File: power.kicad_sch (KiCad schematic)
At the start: 13 parts

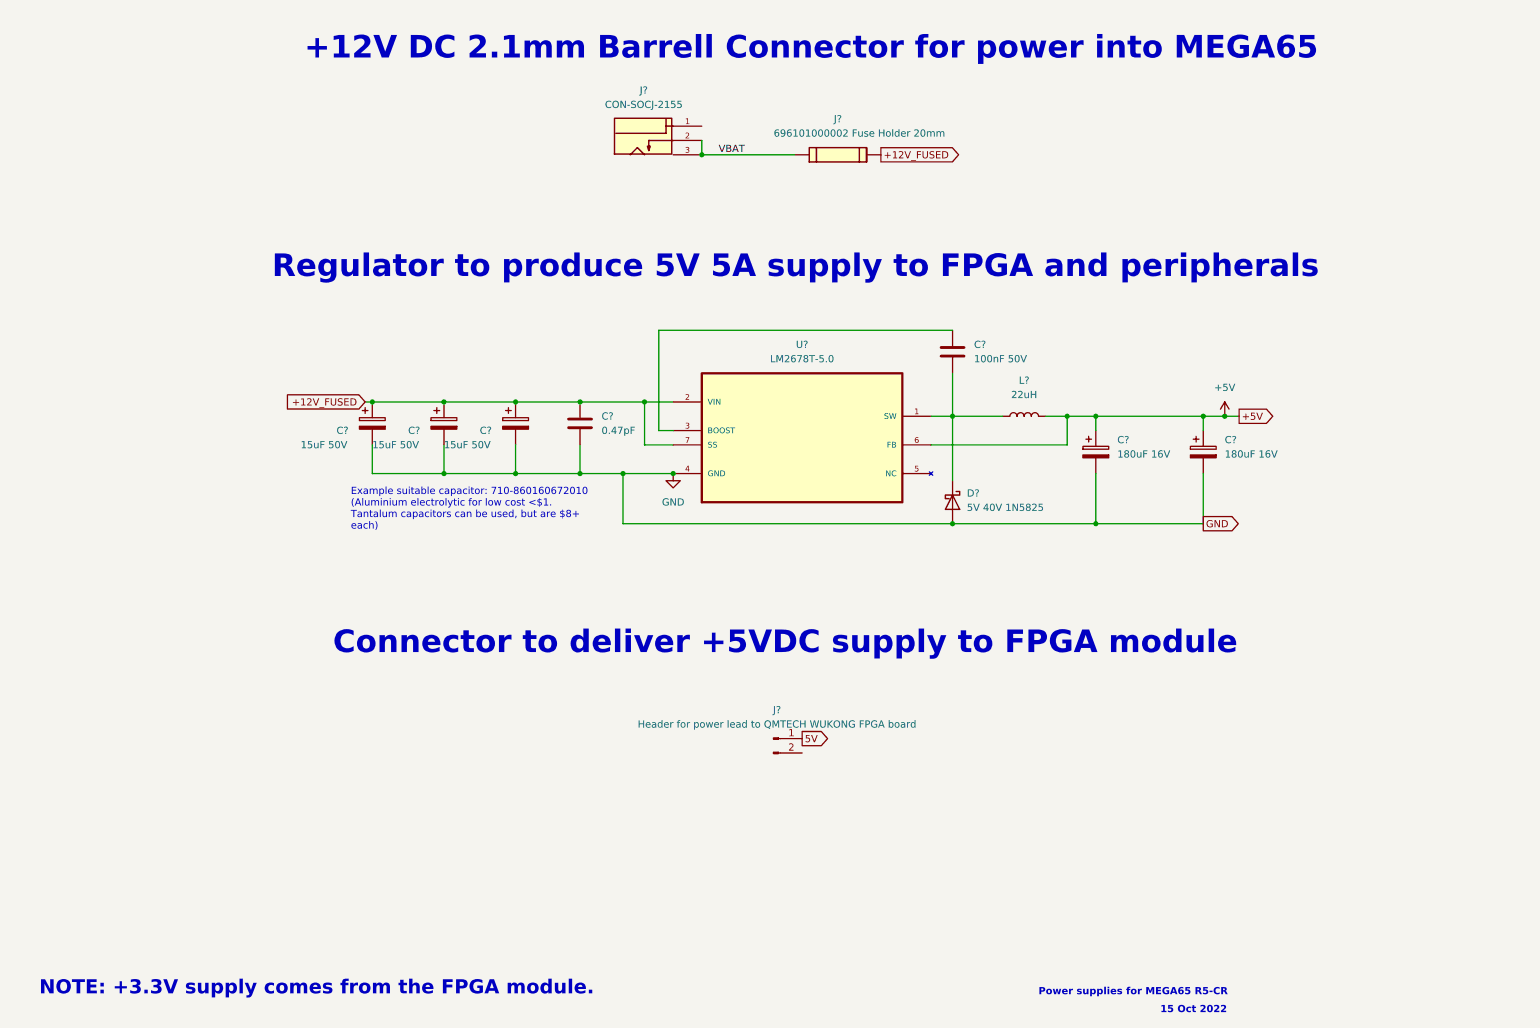
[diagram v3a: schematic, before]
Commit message: add all missing footprints
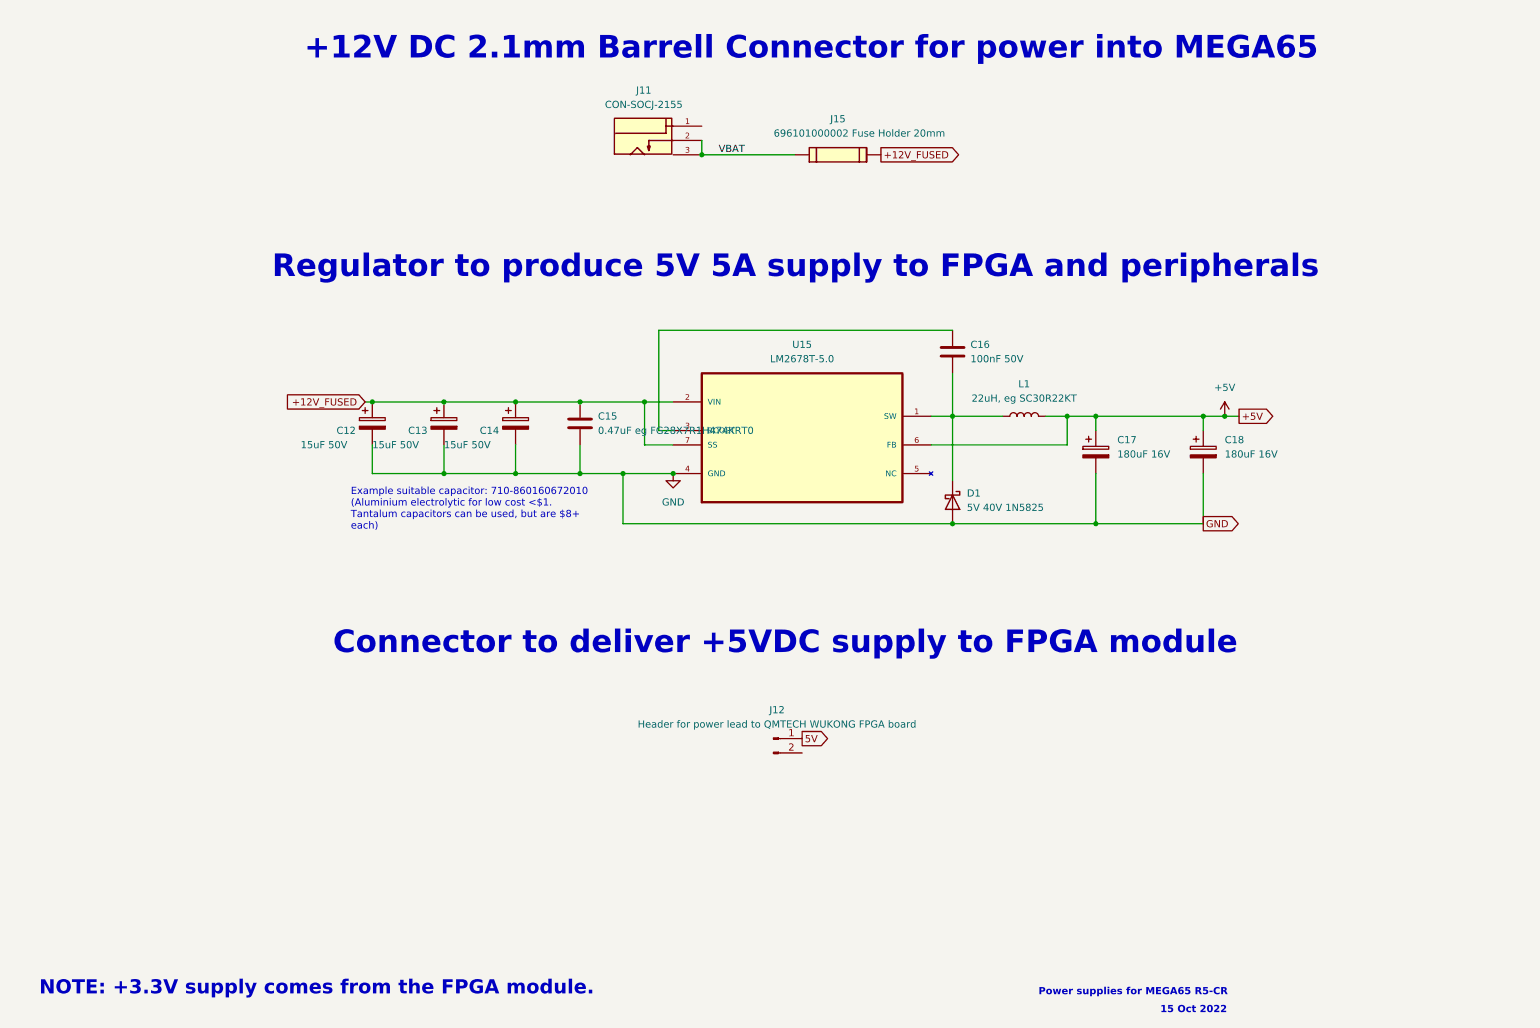
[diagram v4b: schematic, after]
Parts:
- C15: renamed from C?; value 0.47pF -> 0.47uF eg FG28X7R1H474KRT0; footprint (none) -> Capacitor_THT:C_Disc_D6.0mm_W4.4mm_P5.00mm
- C16: renamed from C?; footprint (none) -> Capacitor_THT:C_Disc_D6.0mm_W4.4mm_P5.00mm
- J12: renamed from J?; footprint (none) -> Connector_PinHeader_2.54mm:PinHeader_1x02_P2.54mm_Vertical
- L1: renamed from L?; value 22uH -> 22uH, eg SC30R22KT; footprint (none) -> Inductor_THT:L_Axial_L5.0mm_D3.6mm_P10.00mm_Horizontal_Murata_BL01RN1A2A2
- gave numbers to parts that had none: 9
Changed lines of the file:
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@@
   (symbol (lib_id "Device:C_Polarized") (at 100.965 89.535 0) (unit 1)
     (in_bom yes) (on_board yes)
-    (property "Reference" "C?" (id 0) (at 94.615 90.805 0)
+    (property "Reference" "C14" (id 0) (at 94.615 90.805 0)
       (effects (font (size 1.27 1.27)) (justify left))
     )
@@
   (symbol (lib_id "00Project-SOCJ-2155:CON-SOCJ-2155") (at 123.825 39.37 0) (unit 1)
     (in_bom yes) (on_board yes) (fields_autoplaced)
-    (property "Reference" "J?" (id 0) (at 123.698 30.48 0))
+    (property "Reference" "J11" (id 0) (at 123.698 30.48 0))
     (property "Value" "CON-SOCJ-2155" (id 1) (at 123.698 33.02 0))
     (property "Footprint" "GRAVITECH_CON-SOCJ-2155" (id 2) (at 123.825 39.37 0)
@@
   (symbol (lib_id "Device:C_Polarized") (at 75.565 89.535 0) (unit 1)
     (in_bom yes) (on_board yes)
-    (property "Reference" "C?" (id 0) (at 69.215 90.805 0)
+    (property "Reference" "C12" (id 0) (at 69.215 90.805 0)
       (effects (font (size 1.27 1.27)) (justify left))
     )
@@
   (symbol (lib_id "Device:L") (at 191.135 88.265 90) (unit 1)
     (in_bom yes) (on_board yes) (fields_autoplaced)
-    (property "Reference" "L?" (id 0) (at 191.135 81.915 90))
-    (property "Value" "22uH" (id 1) (at 191.135 84.455 90))
-    (property "Footprint" "" (id 2) (at 191.135 88.265 0)
-      (effects (font (size 1.27 1.27)) hide)
-    )
-    (property "Datasheet" "~" (id 3) (at 191.135 88.265 0)
+    (property "Reference" "L1" (id 0) (at 191.135 82.55 90))
+    (property "Value" "22uH, eg SC30R22KT" (id 1) (at 191.135 85.09 90))
+    (property "Footprint" "Inductor_THT:L_Axial_L5.0mm_D3.6mm_P10.00mm_Horizontal_Murata_BL01RN1A2A2" (id 2) (at 191.135 88.265 0)
+      (effects (font (size 1.27 1.27)) hide)
+    )
+    (property "Datasheet" "https://au.mouser.com/datasheet/2/418/4/NG_DS_1773282_D-725857.pdf" (id 3) (at 191.135 88.265 0)
       (effects (font (size 1.27 1.27)) hide)
     )
@@
   (symbol (lib_id "Device:C") (at 178.435 76.835 0) (unit 1)
     (in_bom yes) (on_board yes) (fields_autoplaced)
-    (property "Reference" "C?" (id 0) (at 182.245 75.5649 0)
-      (effects (font (size 1.27 1.27)) (justify left))
-    )
-    (property "Value" "100nF 50V" (id 1) (at 182.245 78.1049 0)
-      (effects (font (size 1.27 1.27)) (justify left))
-    )
-    (property "Footprint" "" (id 2) (at 179.4002 80.645 0)
+    (property "Reference" "C16" (id 0) (at 181.61 75.5649 0)
+      (effects (font (size 1.27 1.27)) (justify left))
+    )
+    (property "Value" "100nF 50V" (id 1) (at 181.61 78.1049 0)
+      (effects (font (size 1.27 1.27)) (justify left))
+    )
+    (property "Footprint" "Capacitor_THT:C_Disc_D6.0mm_W4.4mm_P5.00mm" (id 2) (at 179.4002 80.645 0)
       (effects (font (size 1.27 1.27)) hide)
     )
@@
   (symbol (lib_id "Device:C_Polarized") (at 222.885 94.615 0) (unit 1)
     (in_bom yes) (on_board yes) (fields_autoplaced)
-    (property "Reference" "C?" (id 0) (at 226.695 92.4559 0)
+    (property "Reference" "C18" (id 0) (at 226.695 92.4559 0)
       (effects (font (size 1.27 1.27)) (justify left))
     )
@@
   (symbol (lib_id "power:+5V") (at 226.695 88.265 0) (unit 1)
     (in_bom yes) (on_board yes) (fields_autoplaced)
-    (property "Reference" "#PWR?" (id 0) (at 226.695 92.075 0)
+    (property "Reference" "#PWR0186" (id 0) (at 226.695 92.075 0)
       (effects (font (size 1.27 1.27)) hide)
     )
@@
   (symbol (lib_id "power:GND") (at 128.905 98.425 0) (unit 1)
     (in_bom yes) (on_board yes) (fields_autoplaced)
-    (property "Reference" "#PWR?" (id 0) (at 128.905 104.775 0)
+    (property "Reference" "#PWR0185" (id 0) (at 128.905 104.775 0)
       (effects (font (size 1.27 1.27)) hide)
     )
@@
   (symbol (lib_id "Connector:Conn_01x02_Male") (at 146.685 145.415 0) (unit 1)
     (in_bom yes) (on_board yes) (fields_autoplaced)
-    (property "Reference" "J?" (id 0) (at 147.32 140.335 0))
+    (property "Reference" "J12" (id 0) (at 147.32 140.335 0))
     (property "Value" "Header for power lead to QMTECH WUKONG FPGA board" (id 1) (at 147.32 142.875 0))
-    (property "Footprint" "" (id 2) (at 146.685 145.415 0)
+    (property "Footprint" "Connector_PinHeader_2.54mm:PinHeader_1x02_P2.54mm_Vertical" (id 2) (at 146.685 145.415 0)
       (effects (font (size 1.27 1.27)) hide)
     )
@@
   (symbol (lib_id "Device:C_Polarized") (at 203.835 94.615 0) (unit 1)
     (in_bom yes) (on_board yes) (fields_autoplaced)
-    (property "Reference" "C?" (id 0) (at 207.645 92.4559 0)
+    (property "Reference" "C17" (id 0) (at 207.645 92.4559 0)
       (effects (font (size 1.27 1.27)) (justify left))
     )
@@
   (symbol (lib_id "00Project-FuseHolder:696101000002") (at 158.115 41.91 0) (unit 1)
     (in_bom yes) (on_board yes)
-    (property "Reference" "J?" (id 0) (at 158.115 35.56 0))
+    (property "Reference" "J15" (id 0) (at 158.115 35.56 0))
     (property "Value" "696101000002 Fuse Holder 20mm" (id 1) (at 161.925 38.1 0))
     (property "Footprint" "696101000002" (id 2) (at 158.115 41.91 0)
@@
   (symbol (lib_id "00Project-5VReg:LM2678T-5.0") (at 151.765 88.265 0) (unit 1)
     (in_bom yes) (on_board yes) (fields_autoplaced)
-    (property "Reference" "U?" (id 0) (at 151.765 75.565 0))
+    (property "Reference" "U15" (id 0) (at 151.765 75.565 0))
     (property "Value" "LM2678T-5.0" (id 1) (at 151.765 78.105 0))
     (property "Footprint" "TO127P457X1016X2052-7P" (id 2) (at 151.765 88.265 0)
@@
   (symbol (lib_id "Device:C_Polarized") (at 88.265 89.535 0) (unit 1)
     (in_bom yes) (on_board yes)
-    (property "Reference" "C?" (id 0) (at 81.915 90.805 0)
+    (property "Reference" "C13" (id 0) (at 81.915 90.805 0)
       (effects (font (size 1.27 1.27)) (justify left))
     )
@@
   (symbol (lib_id "Device:D_Schottky") (at 178.435 103.505 270) (unit 1)
     (in_bom yes) (on_board yes) (fields_autoplaced)
-    (property "Reference" "D?" (id 0) (at 180.975 101.9174 90)
+    (property "Reference" "D1" (id 0) (at 180.975 101.9174 90)
       (effects (font (size 1.27 1.27)) (justify left))
     )
@@
   (symbol (lib_id "Device:C") (at 112.395 89.535 0) (unit 1)
     (in_bom yes) (on_board yes) (fields_autoplaced)
-    (property "Reference" "C?" (id 0) (at 116.205 88.2649 0)
-      (effects (font (size 1.27 1.27)) (justify left))
-    )
-    (property "Value" "0.47pF" (id 1) (at 116.205 90.8049 0)
-      (effects (font (size 1.27 1.27)) (justify left))
-    )
-    (property "Footprint" "" (id 2) (at 113.3602 93.345 0)
-      (effects (font (size 1.27 1.27)) hide)
-    )
-    (property "Datasheet" "~" (id 3) (at 112.395 89.535 0)
-      (effects (font (size 1.27 1.27)) hide)
-    )
+    (property "Reference" "C15" (id 0) (at 115.57 88.2649 0)
+      (effects (font (size 1.27 1.27)) (justify left))
+    )
+    (property "Value" "0.47uF eg FG28X7R1H474KRT0" (id 1) (at 115.57 90.8049 0)
+      (effects (font (size 1.27 1.27)) (justify left))
+    )
+    (property "Footprint" "Capacitor_THT:C_Disc_D6.0mm_W4.4mm_P5.00mm" (id 2) (at 113.3602 93.345 0)
+      (effects (font (size 1.27 1.27)) hide)
+    )
+    (property "Datasheet" "https://product.tdk.com/system/files/dam/doc/product/capacitor/ceramic/lead-mlcc/catalog/leadmlcc_halogenfree_fg_en.pdf" (id 3) (at 112.395 89.535 0)
+      (effects (font (size 1.27 1.27)) hide)
+    )

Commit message: add mezannine for joystick ports to de-clutter board.
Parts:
- J11: footprint GRAVITECH_CON-SOCJ-2155 -> snapeda:GRAVITECH_CON-SOCJ-2155
- J15: footprint 696101000002 -> snapeda:696101000002
- U15: footprint TO127P457X1016X2052-7P -> snapeda:TO127P457X1016X2052-7P
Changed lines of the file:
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@@
     (property "Reference" "J11" (id 0) (at 123.698 30.48 0))
     (property "Value" "CON-SOCJ-2155" (id 1) (at 123.698 33.02 0))
-    (property "Footprint" "GRAVITECH_CON-SOCJ-2155" (id 2) (at 123.825 39.37 0)
+    (property "Footprint" "snapeda:GRAVITECH_CON-SOCJ-2155" (id 2) (at 123.825 39.37 0)
       (effects (font (size 1.27 1.27)) (justify left bottom) hide)
     )
@@
     (property "Reference" "J15" (id 0) (at 158.115 35.56 0))
     (property "Value" "696101000002 Fuse Holder 20mm" (id 1) (at 161.925 38.1 0))
-    (property "Footprint" "696101000002" (id 2) (at 158.115 41.91 0)
+    (property "Footprint" "snapeda:696101000002" (id 2) (at 158.115 41.91 0)
       (effects (font (size 1.27 1.27)) (justify left bottom) hide)
     )
@@
     (property "Reference" "U15" (id 0) (at 151.765 75.565 0))
     (property "Value" "LM2678T-5.0" (id 1) (at 151.765 78.105 0))
-    (property "Footprint" "TO127P457X1016X2052-7P" (id 2) (at 151.765 88.265 0)
+    (property "Footprint" "snapeda:TO127P457X1016X2052-7P" (id 2) (at 151.765 88.265 0)
       (effects (font (size 1.27 1.27)) (justify left bottom) hide)
     )

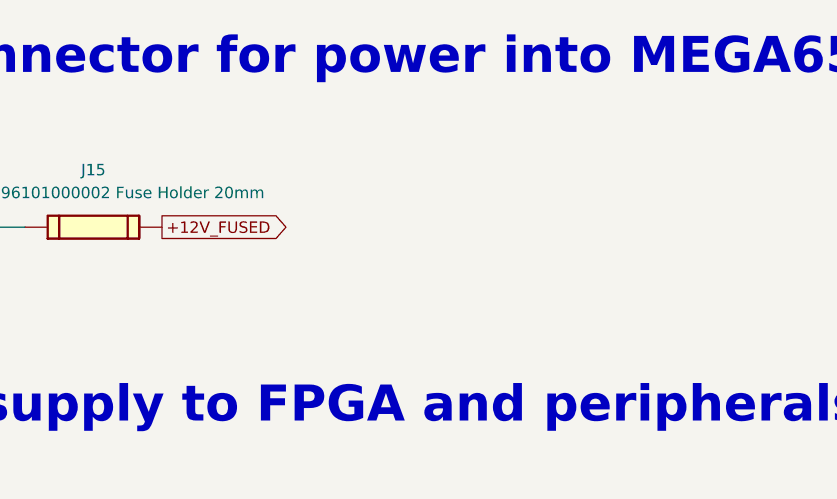
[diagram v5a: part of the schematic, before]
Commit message: add missing power switch #7
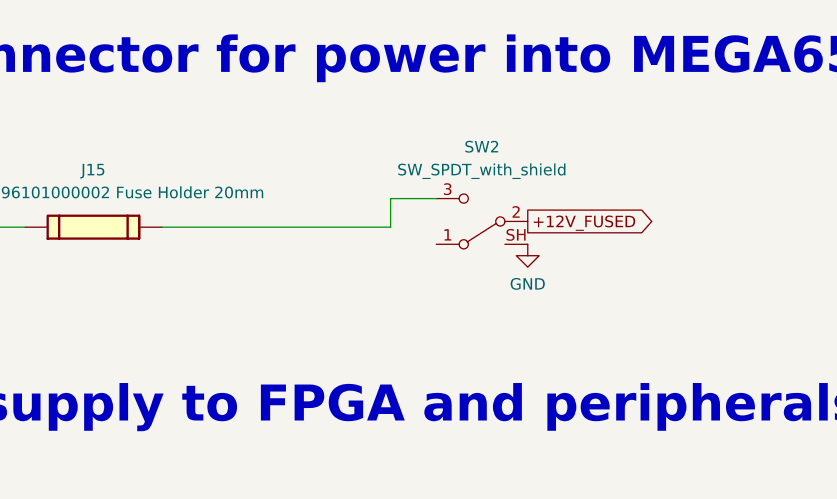
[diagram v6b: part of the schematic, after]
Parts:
- added SW2: SW_SPDT_with_shield, snapeda:T103J1AVBE2, symbol 00Project-SDF-60J:SW_SPDT_with_shield
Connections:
- net +12V_FUSED: now also SW2.2 (B); no longer J15.2
- net GND: now also SW2.SH (SHIELD)
- new net: J15.2, SW2.3 (C)
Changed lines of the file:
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@@
+    (stroke (width 0) (type default) (color 0 0 0 0))
+  )
+  (wire (pts (xy 191.135 38.735) (xy 196.215 38.735))
+    (stroke (width 0) (type default) (color 0 0 0 0))
+  )
+  (wire (pts (xy 191.135 41.91) (xy 191.135 38.735))
     (stroke (width 0) (type default) (color 0 0 0 0))
   )
   (wire (pts (xy 120.015 98.425) (xy 128.905 98.425))
+    (stroke (width 0) (type default) (color 0 0 0 0))
+  )
+  (wire (pts (xy 165.735 41.91) (xy 191.135 41.91))
     (stroke (width 0) (type default) (color 0 0 0 0))
   )
@@
     )
   )
-  (global_label "+12V_FUSED" (shape output) (at 165.735 41.91 0) (fields_autoplaced)
+  (global_label "+12V_FUSED" (shape output) (at 206.375 41.275 0) (fields_autoplaced)
     (effects (font (size 1.27 1.27)) (justify left))
-    (property "Intersheet References" "${INTERSHEET_REFS}" (id 0) (at 180.2433 41.8306 0)
+    (property "Intersheet References" "${INTERSHEET_REFS}" (id 0) (at 220.8833 41.1956 0)
       (effects (font (size 1.27 1.27)) (justify left) hide)
     )
@@
     (pin "2")
   )
+  (symbol (lib_id "00Project-SDF-60J:SW_SPDT_with_shield") (at 201.295 41.275 180) (unit 1)
+    (in_bom yes) (on_board yes) (fields_autoplaced)
+    (property "Reference" "SW2" (id 0) (at 201.295 33.02 0))
+    (property "Value" "SW_SPDT_with_shield" (id 1) (at 201.295 35.56 0))
+    (property "Footprint" "snapeda:T103J1AVBE2" (id 2) (at 201.295 41.275 0)
+      (effects (font (size 1.27 1.27)) hide)
+    )
+    (property "Datasheet" "~" (id 3) (at 201.295 41.275 0)
+      (effects (font (size 1.27 1.27)) hide)
+    )
+    (pin "1")
+    (pin "2")
+    (pin "3")
+    (pin "SH")
+  )
   (symbol (lib_id "Device:C") (at 178.435 76.835 0) (unit 1)
     (in_bom yes) (on_board yes) (fields_autoplaced)
@@
       (effects (font (size 1.27 1.27)) hide)
     )
+    (pin "1")
+  )
+  (symbol (lib_id "power:GND") (at 206.375 43.815 0) (unit 1)
+    (in_bom yes) (on_board yes) (fields_autoplaced)
+    (property "Reference" "#PWR0290" (id 0) (at 206.375 50.165 0)
+      (effects (font (size 1.27 1.27)) hide)
+    )
+    (property "Value" "GND" (id 1) (at 206.375 48.26 0))
+    (property "Footprint" "" (id 2) (at 206.375 43.815 0)
+      (effects (font (size 1.27 1.27)) hide)
+    )
+    (property "Datasheet" "" (id 3) (at 206.375 43.815 0)
+      (effects (font (size 1.27 1.27)) hide)
+    )
